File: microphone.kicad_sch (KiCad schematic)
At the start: 21 parts, among them U1 NMA0515SC

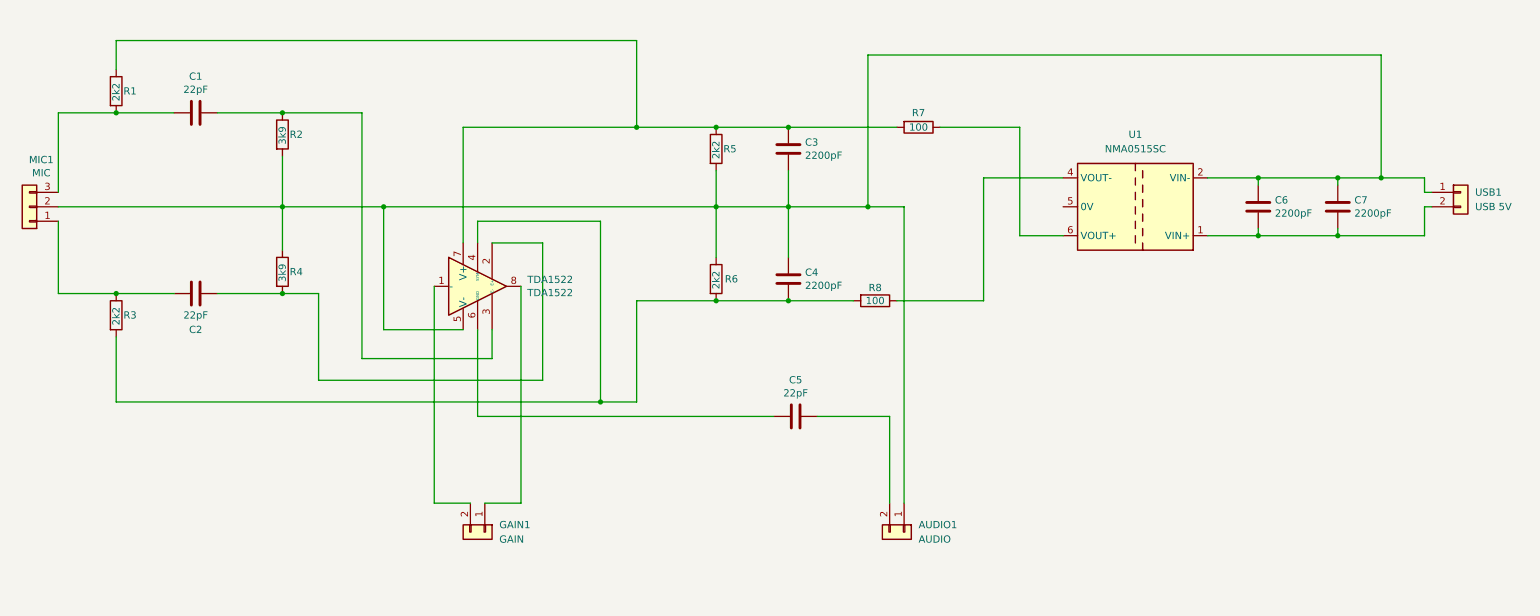
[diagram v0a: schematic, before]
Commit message: Add Mounting Hole symbols and update references in schematic - Created a new design rule file (DRU) with custom DRC settings for PCBWay
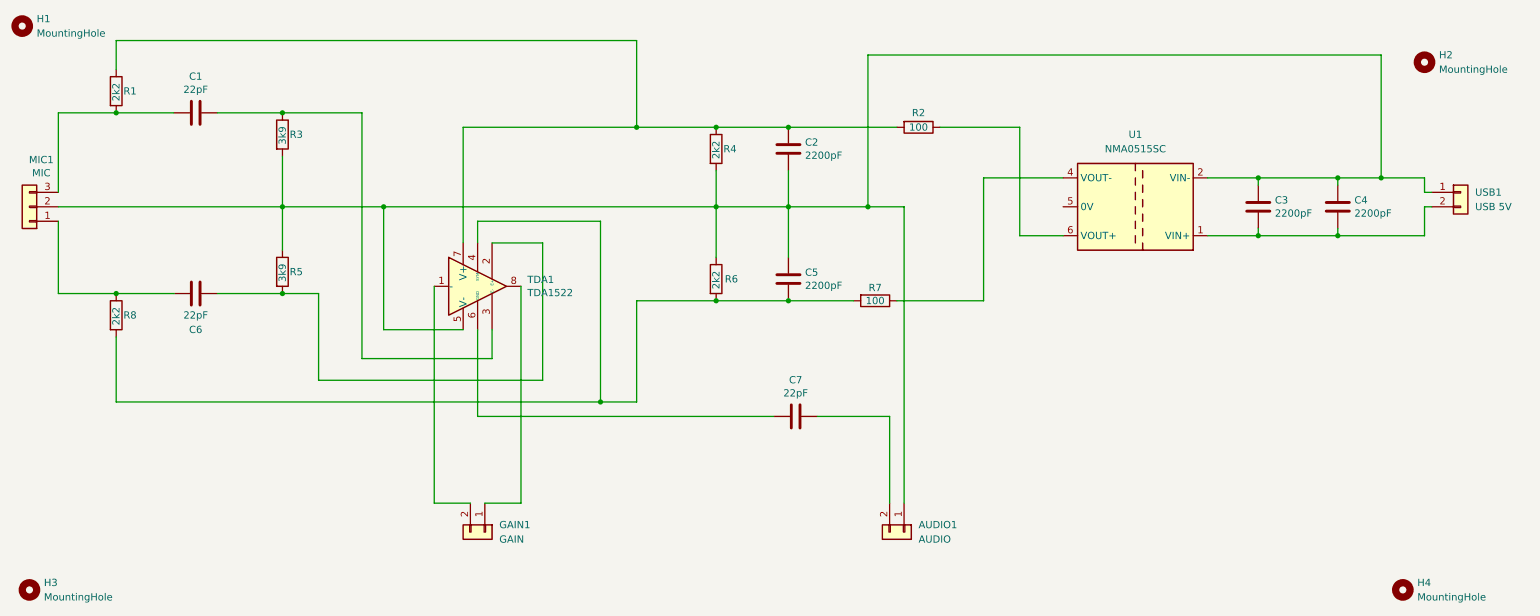
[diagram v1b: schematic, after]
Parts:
- added H1, H2, H3, H4: MountingHole, MountingHole:MountingHole_2.2mm_M2, symbol Mechanical:MountingHole
- renumbered C3 to C2, C6 to C3, C7 to C4, C4 to C5, C2 to C6, C5 to C7, R7 to R2, R2 to R3, R5 to R4, R4 to R5, R8 to R7, R3 to R8, TDA1522 to TDA1
